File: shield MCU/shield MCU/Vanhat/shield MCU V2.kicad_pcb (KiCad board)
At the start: 2 copper layers, 56 x 75.2 mm, 16 parts, among them J1 IR_sensor, J2 IR_sensor, J3 IR_sensor, J4 IR_sensor, J5 IR_sensor, J6 BATT, SW1 Pwr_Sw, U1 pwr_mgr_1, U3 gy50, U4 NUCLEO144-F429ZI

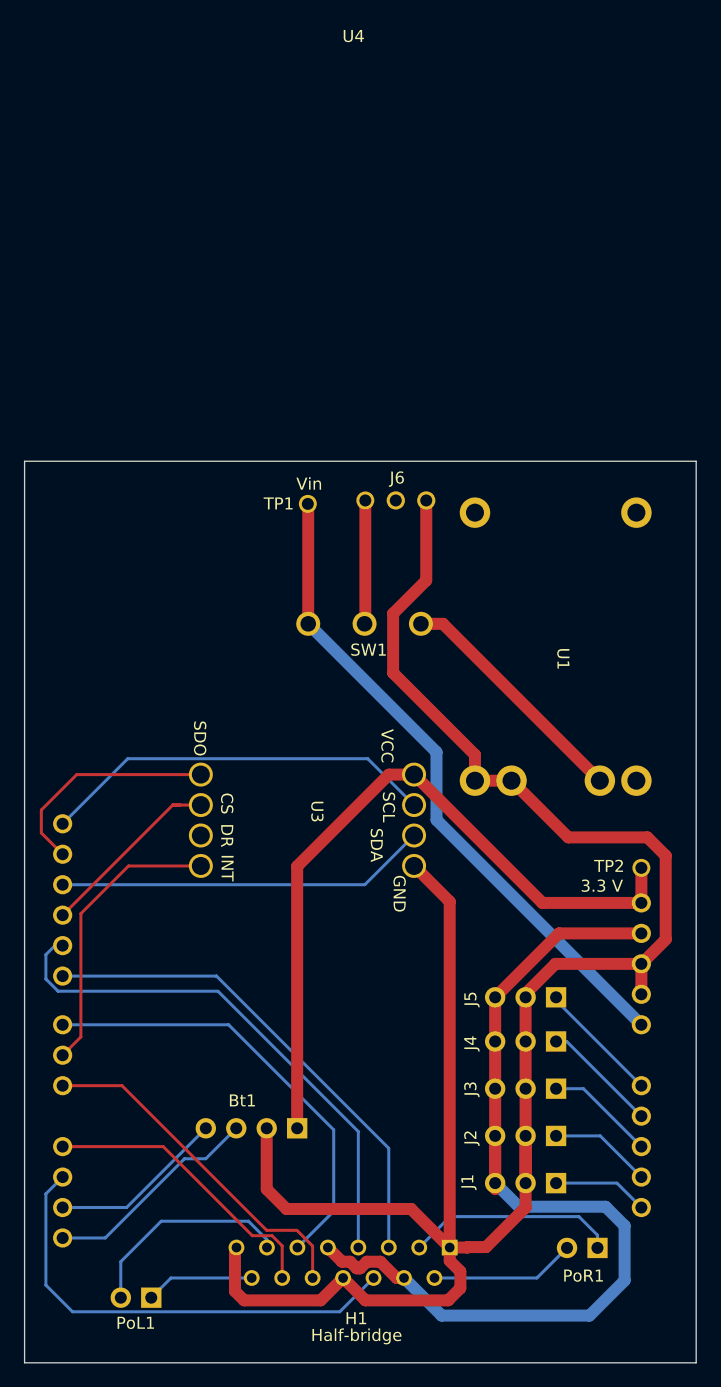
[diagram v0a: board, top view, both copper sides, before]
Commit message: PCB with gnd layer
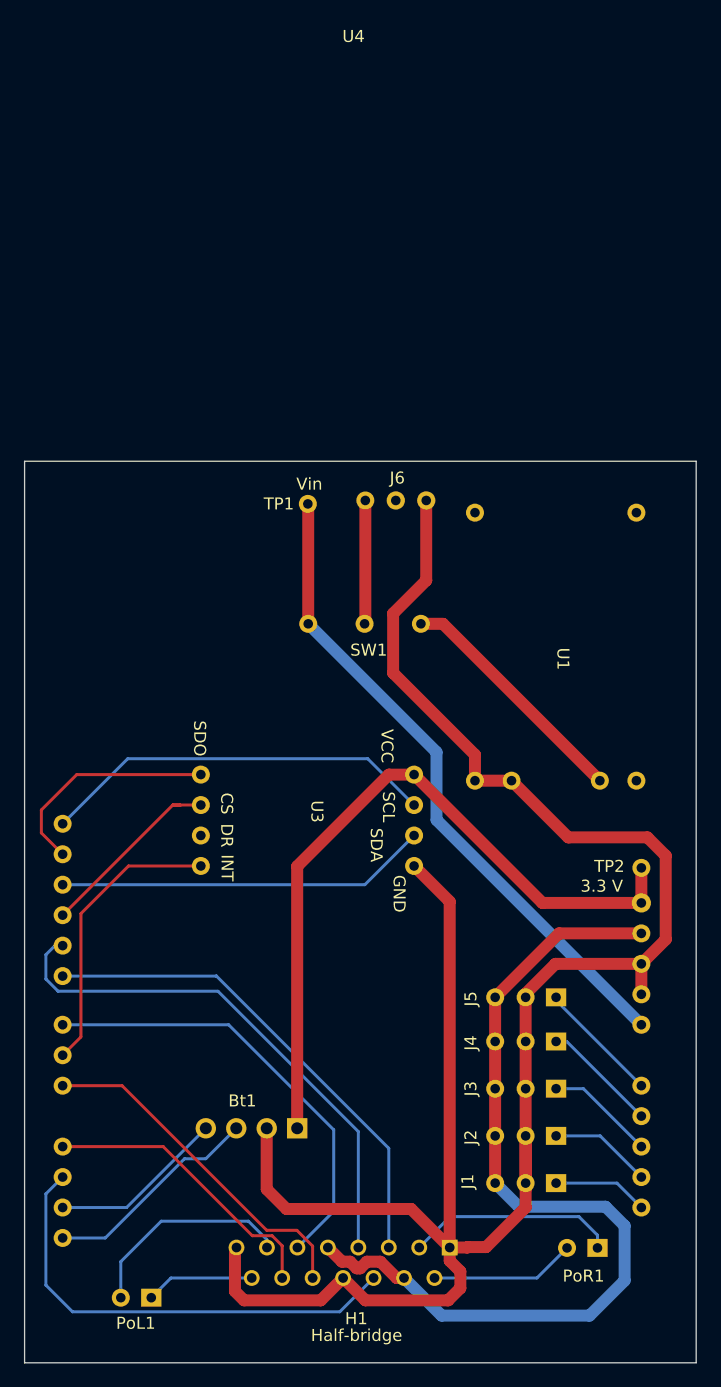
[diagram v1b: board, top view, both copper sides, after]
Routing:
- net /5V: track 79.4 -> 75.5 mm
